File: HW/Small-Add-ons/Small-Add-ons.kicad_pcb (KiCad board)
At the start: 2 copper layers, 51 parts, among them P100 PVIn, P101 PVOut, P110 PWMin, P111 PVOut, P112 PVOut, P113 PVOut, P120 PLVLC, P121 PLVLC, P130 loConn, P131 hiConn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

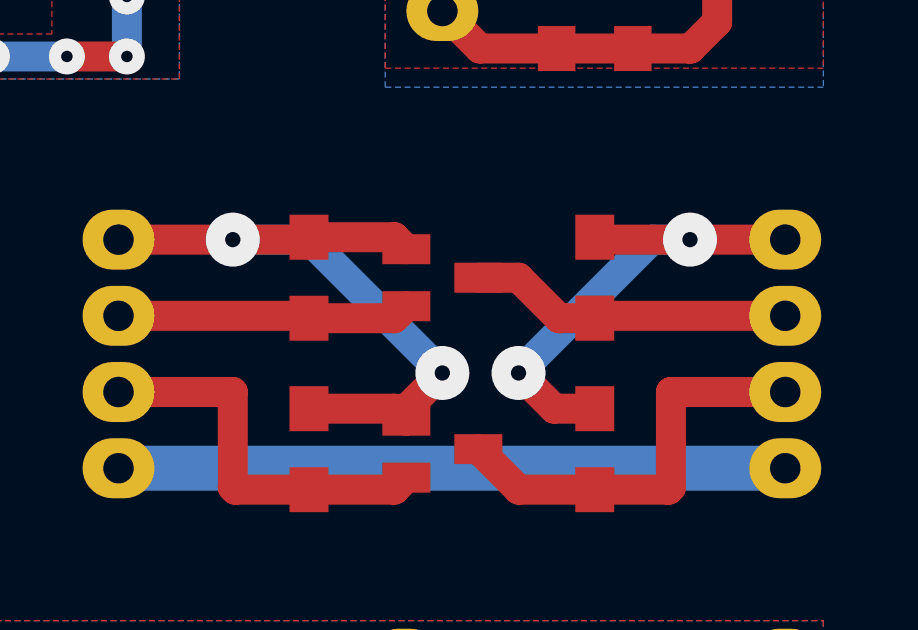
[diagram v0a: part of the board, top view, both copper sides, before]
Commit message: License info added to .h and .cpp files and README update
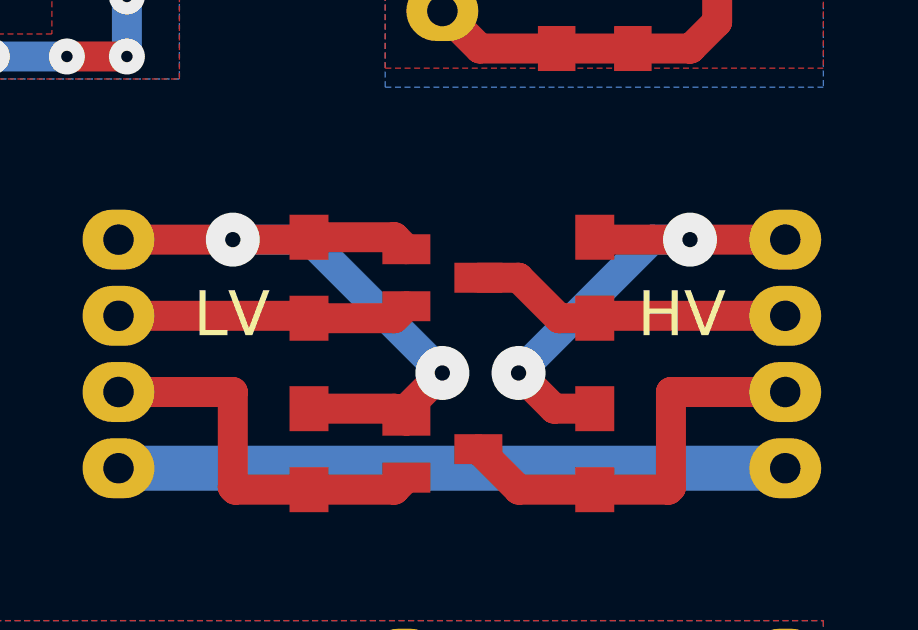
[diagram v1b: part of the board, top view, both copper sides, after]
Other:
- board text added: "HV"
- board text added: "LV"
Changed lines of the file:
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@@
     (area 27.336905 15.76 108.925 61.015)
     (thickness 1.6)
-    (drawings 9)
+    (drawings 11)
     (tracks 323)
     (zones 0)
@@
   )
   (setup
-    (last_trace_width 1)
+    (last_trace_width 0.5)
     (user_trace_width 0.6)
     (user_trace_width 0.7)
@@
       (net 40 "Net-(P60-Pad1)"))
   )
+  (gr_text HV (at 67.85 38.23) (layer F.SilkS)
+    (effects (font (size 1.5 1.5) (thickness 0.3)))
+  )
+  (gr_text LV (at 52.85 38.23) (layer F.SilkS)
+    (effects (font (size 1.5 1.5) (thickness 0.3)))
+  )
   (gr_text -VIn+ (at 98.605 37.01 90) (layer F.SilkS)

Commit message: Added pin names for level convertor board
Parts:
- moved P120 3.00 mm to (26.8, 35.9)
- moved P121 3.00 mm to (37.8, 43.4)
- moved U120 3.00 mm to (32.3, 41.7)
- moved U121 3.00 mm to (32.3, 37.7)
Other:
- board text added: "Gnd"
- board text added: "In"
- board text added: "Out"
- board text added: "Vcc"
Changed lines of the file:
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@@
     (area 27.336905 15.76 108.925 61.015)
     (thickness 1.6)
-    (drawings 11)
+    (drawings 20)
     (tracks 323)
     (zones 0)
@@
   )
   (module Calin:Pin_Header_Straight_1x04 (layer B.Cu)
-    (at 29.825 35.91 180)
+    (at 26.825 35.91 180)
     (descr "Through hole pin header")
     (tags "pin header")
@@
   )
   (module Calin:Pin_Header_Straight_1x04 (layer B.Cu)
-    (at 40.825 43.41)
+    (at 37.825 43.41)
     (descr "Through hole pin header")
     (tags "pin header")
@@
   )
   (module Calin:SOT23-5 (layer F.Cu)
-    (at 35.325 37.66 90)
+    (at 32.325 37.66 90)
     (fp_text reference U121 (at 0 3 90) (layer F.Fab)
       (effects (font (size 1 1) (thickness 0.15)))
@@
   )
   (module Calin:SOT23-5 (layer F.Cu)
-    (at 35.325 41.66 270)
+    (at 32.325 41.66 270)
     (fp_text reference U120 (at 0 3 270) (layer F.Fab)
       (effects (font (size 1 1) (thickness 0.15)))
@@
     (pad 4 smd rect (at 2.7 -1.6 90) (size 2 1) (layers F.Cu F.Paste F.Mask)
       (net 40 "Net-(P60-Pad1)"))
+  )
+  (gr_text Gnd (at 41.85 35.23) (layer Dwgs.User)
+    (effects (font (size 1.5 1.5) (thickness 0.3)))
+  )
+  (gr_text In (at 40.85 37.73) (layer Dwgs.User)
+    (effects (font (size 1.5 1.5) (thickness 0.3)))
+  )
+  (gr_text Vcc (at 41.85 41.73) (layer Dwgs.User)
+    (effects (font (size 1.5 1.5) (thickness 0.3)))
+  )
+  (gr_text Out (at 41.85 44.23) (layer Dwgs.User)
+    (effects (font (size 1.5 1.5) (thickness 0.3)))
+  )
+  (gr_line (start 40.85 39.73) (end 23.35 39.73) (angle 90) (layer Dwgs.User) (width 0.2))
+  (gr_text Out (at 22.85 35.23) (layer Dwgs.User)
+    (effects (font (size 1.5 1.5) (thickness 0.3)))
+  )
+  (gr_text Vcc (at 22.85 37.73) (layer Dwgs.User)
+    (effects (font (size 1.5 1.5) (thickness 0.3)))
+  )
+  (gr_text In (at 23.85 41.73) (layer Dwgs.User)
+    (effects (font (size 1.5 1.5) (thickness 0.3)))
+  )
+  (gr_text Gnd (at 22.85 44.23) (layer Dwgs.User)
+    (effects (font (size 1.5 1.5) (thickness 0.3)))
   )
   (gr_text HV (at 67.85 38.23) (layer F.SilkS)
@@
   (segment (start 87.81 39.55) (end 87.81 42.09) (width 1.5) (layer B.Cu) (net 7))
   (via (at 87.81 39.55) (size 1.2) (drill 0.381) (layers F.Cu B.Cu) (net 7))
-  (segment (start 33.975 36.71) (end 32.625 36.71) (width 0.6) (layer F.Cu) (net 8))
-  (segment (start 31.825 35.91) (end 29.825 35.91) (width 1.2) (layer F.Cu) (net 8))
-  (segment (start 32.625 36.71) (end 31.825 35.91) (width 0.6) (layer F.Cu) (net 8))
-  (segment (start 33.975 38.61) (end 31.825 38.61) (width 0.6) (layer F.Cu) (net 9))
-  (segment (start 31.825 38.61) (end 29.985 38.61) (width 1.2) (layer F.Cu) (net 9))
-  (segment (start 29.985 38.61) (end 29.825 38.45) (width 0.6) (layer F.Cu) (net 9))
-  (segment (start 33.975 41.66) (end 32.575 41.66) (width 0.6) (layer F.Cu) (net 10))
-  (segment (start 31.905 40.99) (end 29.825 40.99) (width 1.2) (layer F.Cu) (net 10))
-  (segment (start 32.575 41.66) (end 31.905 40.99) (width 0.6) (layer F.Cu) (net 10))
-  (segment (start 33.975 42.61) (end 32.365 42.61) (width 0.6) (layer F.Cu) (net 11))
-  (segment (start 32.365 42.61) (end 31.445 43.53) (width 0.6) (layer F.Cu) (net 11))
-  (segment (start 36.675 36.71) (end 38.285 36.71) (width 0.6) (layer F.Cu) (net 11))
-  (segment (start 38.285 36.71) (end 39.205 35.79) (width 0.6) (layer F.Cu) (net 11))
-  (segment (start 29.825 43.53) (end 31.445 43.53) (width 1.2) (layer F.Cu) (net 11))
-  (segment (start 39.205 35.79) (end 38.325 34.91) (width 1.2) (layer F.Cu) (net 11))
-  (segment (start 31.445 43.53) (end 32.325 44.41) (width 1.2) (layer F.Cu) (net 11))
-  (segment (start 32.325 44.41) (end 35.325 44.41) (width 1.2) (layer F.Cu) (net 11))
-  (via (at 35.325 44.41) (size 1.2) (drill 0.381) (layers F.Cu B.Cu) (net 11))
-  (segment (start 35.325 34.91) (end 35.325 44.41) (width 1.2) (layer B.Cu) (net 11))
-  (via (at 35.325 34.91) (size 1.2) (drill 0.381) (layers F.Cu B.Cu) (net 11))
-  (segment (start 38.325 34.91) (end 35.325 34.91) (width 1.2) (layer F.Cu) (net 11))
-  (segment (start 39.205 35.79) (end 40.825 35.79) (width 1.2) (layer F.Cu) (net 11))
-  (segment (start 33.975 42.61) (end 33.625 42.61) (width 0.6) (layer F.Cu) (net 11))
-  (segment (start 36.675 42.61) (end 38.025 42.61) (width 0.6) (layer F.Cu) (net 12))
-  (segment (start 38.825 43.41) (end 40.825 43.41) (width 1.2) (layer F.Cu) (net 12))
-  (segment (start 38.025 42.61) (end 38.825 43.41) (width 0.6) (layer F.Cu) (net 12))
-  (segment (start 36.675 40.71) (end 38.825 40.71) (width 0.6) (layer F.Cu) (net 13))
-  (segment (start 38.825 40.71) (end 40.665 40.71) (width 1.2) (layer F.Cu) (net 13))
-  (segment (start 40.665 40.71) (end 40.825 40.87) (width 0.6) (layer F.Cu) (net 13))
-  (segment (start 36.675 37.66) (end 38.075 37.66) (width 0.6) (layer F.Cu) (net 14))
-  (segment (start 38.745 38.33) (end 40.825 38.33) (width 1.2) (layer F.Cu) (net 14))
-  (segment (start 38.075 37.66) (end 38.745 38.33) (width 0.6) (layer F.Cu) (net 14))
+  (segment (start 30.975 36.71) (end 29.625 36.71) (width 0.6) (layer F.Cu) (net 8))
+  (segment (start 28.825 35.91) (end 26.825 35.91) (width 1.2) (layer F.Cu) (net 8))
+  (segment (start 29.625 36.71) (end 28.825 35.91) (width 0.6) (layer F.Cu) (net 8))
+  (segment (start 30.975 38.61) (end 28.825 38.61) (width 0.6) (layer F.Cu) (net 9))
+  (segment (start 28.825 38.61) (end 26.985 38.61) (width 1.2) (layer F.Cu) (net 9))
+  (segment (start 26.985 38.61) (end 26.825 38.45) (width 0.6) (layer F.Cu) (net 9))
+  (segment (start 30.975 41.66) (end 29.575 41.66) (width 0.6) (layer F.Cu) (net 10))
+  (segment (start 28.905 40.99) (end 26.825 40.99) (width 1.2) (layer F.Cu) (net 10))
+  (segment (start 29.575 41.66) (end 28.905 40.99) (width 0.6) (layer F.Cu) (net 10))
+  (segment (start 30.975 42.61) (end 29.365 42.61) (width 0.6) (layer F.Cu) (net 11))
+  (segment (start 29.365 42.61) (end 28.445 43.53) (width 0.6) (layer F.Cu) (net 11))
+  (segment (start 33.675 36.71) (end 35.285 36.71) (width 0.6) (layer F.Cu) (net 11))
+  (segment (start 35.285 36.71) (end 36.205 35.79) (width 0.6) (layer F.Cu) (net 11))
+  (segment (start 26.825 43.53) (end 28.445 43.53) (width 1.2) (layer F.Cu) (net 11))
+  (segment (start 36.205 35.79) (end 35.325 34.91) (width 1.2) (layer F.Cu) (net 11))
+  (segment (start 28.445 43.53) (end 29.325 44.41) (width 1.2) (layer F.Cu) (net 11))
+  (segment (start 29.325 44.41) (end 32.325 44.41) (width 1.2) (layer F.Cu) (net 11))
+  (via (at 32.325 44.41) (size 1.2) (drill 0.381) (layers F.Cu B.Cu) (net 11))
+  (segment (start 32.325 34.91) (end 32.325 44.41) (width 1.2) (layer B.Cu) (net 11))
+  (via (at 32.325 34.91) (size 1.2) (drill 0.381) (layers F.Cu B.Cu) (net 11))
+  (segment (start 35.325 34.91) (end 32.325 34.91) (width 1.2) (layer F.Cu) (net 11))
+  (segment (start 36.205 35.79) (end 37.825 35.79) (width 1.2) (layer F.Cu) (net 11))
+  (segment (start 30.975 42.61) (end 30.625 42.61) (width 0.6) (layer F.Cu) (net 11))
+  (segment (start 33.675 42.61) (end 35.025 42.61) (width 0.6) (layer F.Cu) (net 12))
+  (segment (start 35.825 43.41) (end 37.825 43.41) (width 1.2) (layer F.Cu) (net 12))
+  (segment (start 35.025 42.61) (end 35.825 43.41) (width 0.6) (layer F.Cu) (net 12))
+  (segment (start 33.675 40.71) (end 35.825 40.71) (width 0.6) (layer F.Cu) (net 13))
+  (segment (start 35.825 40.71) (end 37.665 40.71) (width 1.2) (layer F.Cu) (net 13))
+  (segment (start 37.665 40.71) (end 37.825 40.87) (width 0.6) (layer F.Cu) (net 13))
+  (segment (start 33.675 37.66) (end 35.075 37.66) (width 0.6) (layer F.Cu) (net 14))
+  (segment (start 35.745 38.33) (end 37.825 38.33) (width 1.2) (layer F.Cu) (net 14))
+  (segment (start 35.075 37.66) (end 35.745 38.33) (width 0.6) (layer F.Cu) (net 14))
   (segment (start 94.16 44.63) (end 103.05 44.63) (width 2) (layer B.Cu) (net 15) (status 20))
   (segment (start 87.81 44.63) (end 80.825 44.63) (width 2) (layer B.Cu) (net 16))
@@
     (polygon
       (pts
-        (xy 28.325 34.41) (xy 42.325 34.41) (xy 42.325 44.91) (xy 28.325 44.91)
+        (xy 25.325 34.41) (xy 39.325 34.41) (xy 39.325 44.91) (xy 25.325 44.91)
       )
     )
